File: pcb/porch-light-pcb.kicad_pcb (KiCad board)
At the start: 2 copper layers, 67 x 44 mm, 11 parts, among them J1 1-2834011-3, J2 Conn_01x02, K1 PRY2-3V-450-1A-EF, Q1 PN2222A

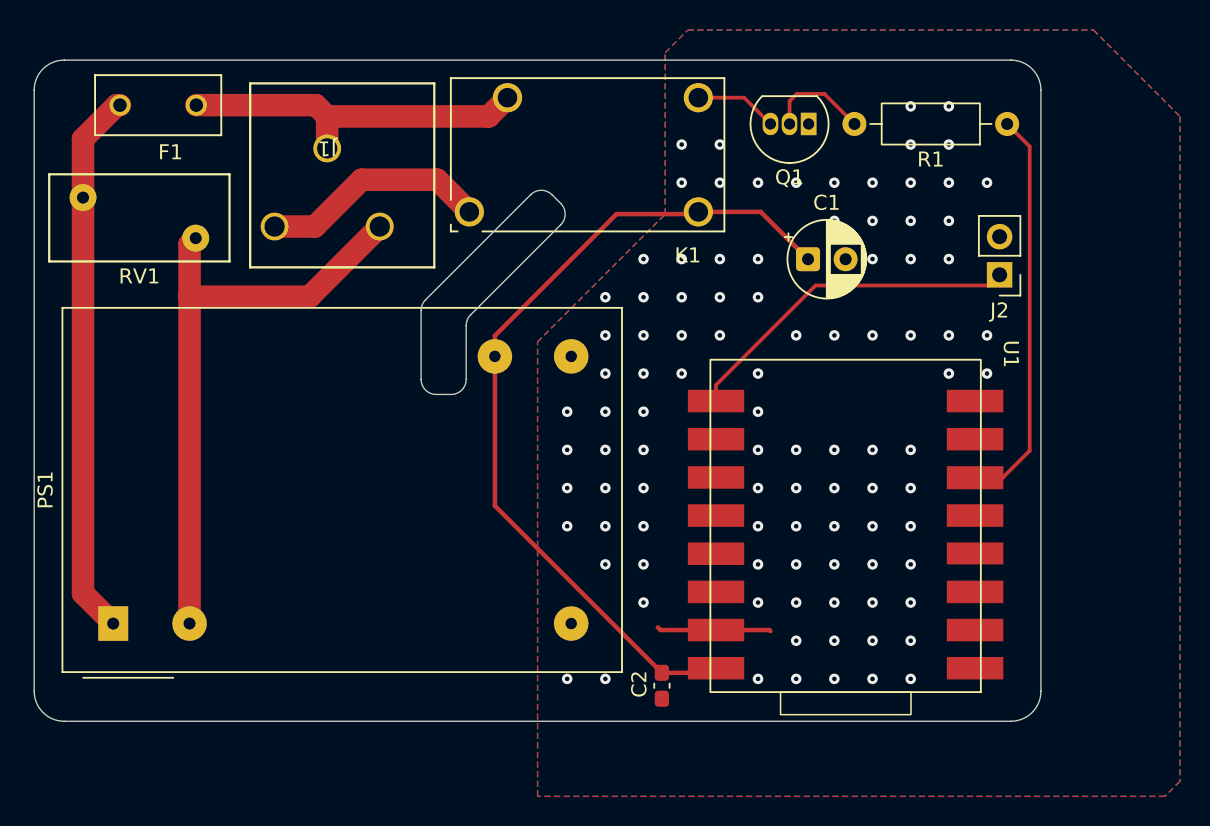
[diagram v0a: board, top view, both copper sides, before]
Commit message: added flyback diode to relay
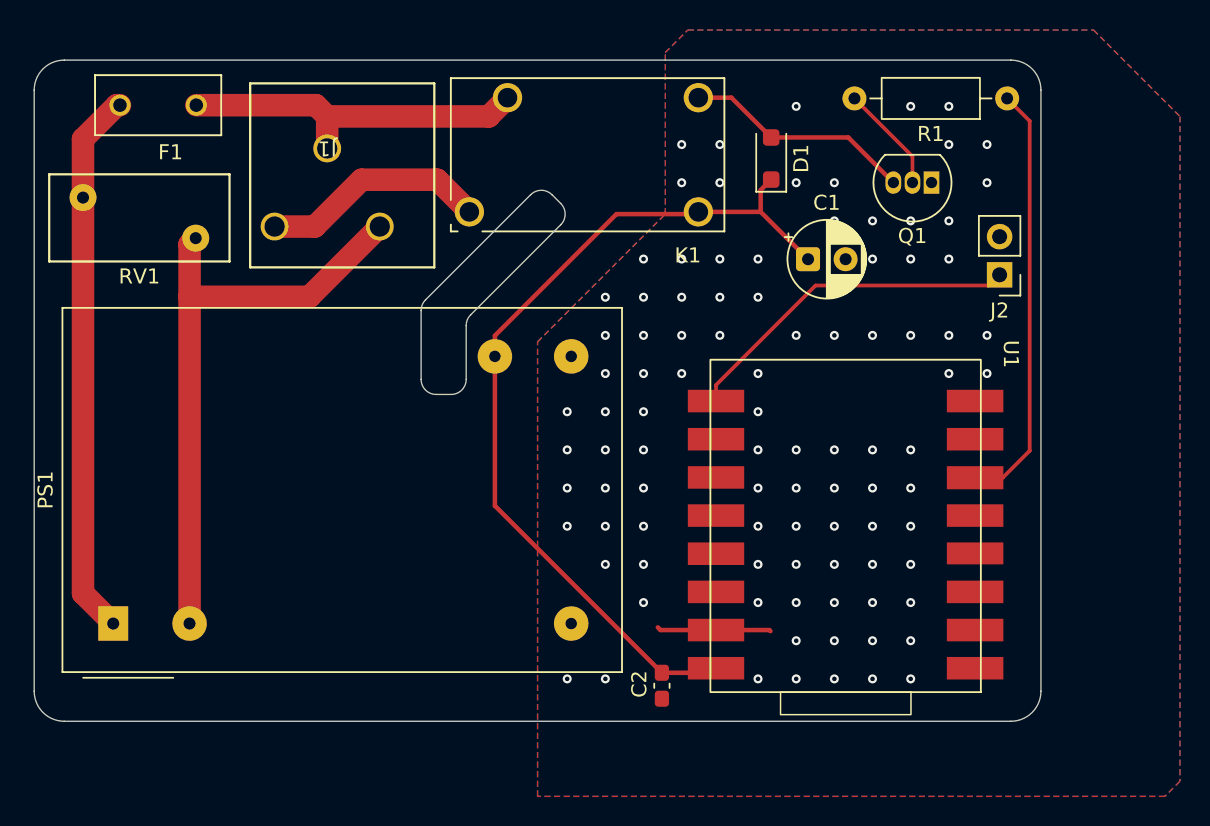
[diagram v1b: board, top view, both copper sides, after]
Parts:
- added D1: 1N4007, Diode_SMD:D_SOD-123F, F.Cu at (135.3, 42.3)
- moved Q1 9.06 mm to (146.0, 43.9)
- moved R1 1.70 mm to (151.0, 38.3)
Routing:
- net /RELAY_GND: track 5.52 -> 15.3 mm
- net +3.3V: track 56.3 -> 58.8 mm
- net /RELAY_GPIO: track 26.7 -> 28.4 mm
- net GND: vias 99 -> 96

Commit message: swapped 220uF for 47uF, added jumper to disable USB power
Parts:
- added J3: Conn_01x02, Connector_PinHeader_2.54mm:PinHeader_1x02_P2.54mm_Vertical, F.Cu at (127.5, 74.1)
- C1: value 220uF -> 47uF; footprint Capacitor_THT:CP_Radial_D5.0mm_P2.50mm -> Capacitor_THT:CP_Radial_D4.0mm_P1.50mm
- moved U1 0.75 mm to (141.3, 65.8)
- moved C2 0.63 mm to (128.6, 77.7), turned to 90 degrees
- moved C1 0.15 mm to (137.9, 49.0)
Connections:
- C2 pad 1: +3.3V -> GND
- C2 pad 2: GND -> Net-(J3-Pin_1)
- U1 pad 16: +3.3V -> Net-(J3-Pin_1)
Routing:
- net +3.3V: track 58.8 -> 51.1 mm
- net Net-(J3-Pin_1): track 0.00 -> 6.71 mm
- net /RELAY_GPIO: track 28.4 -> 27.7 mm
- net /BUTTON_GPIO: track 23.0 -> 22.5 mm
- net GND: track 7.60 -> 7.14 mm, vias 96 -> 86
